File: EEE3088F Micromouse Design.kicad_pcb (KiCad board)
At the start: 2 copper layers, 70 x 78.3 mm, 10 parts, among them J1 Conn_02x16_Odd_Even, J2 Conn_01x02, SW1 SW_SPDT, U1 INA219AxD

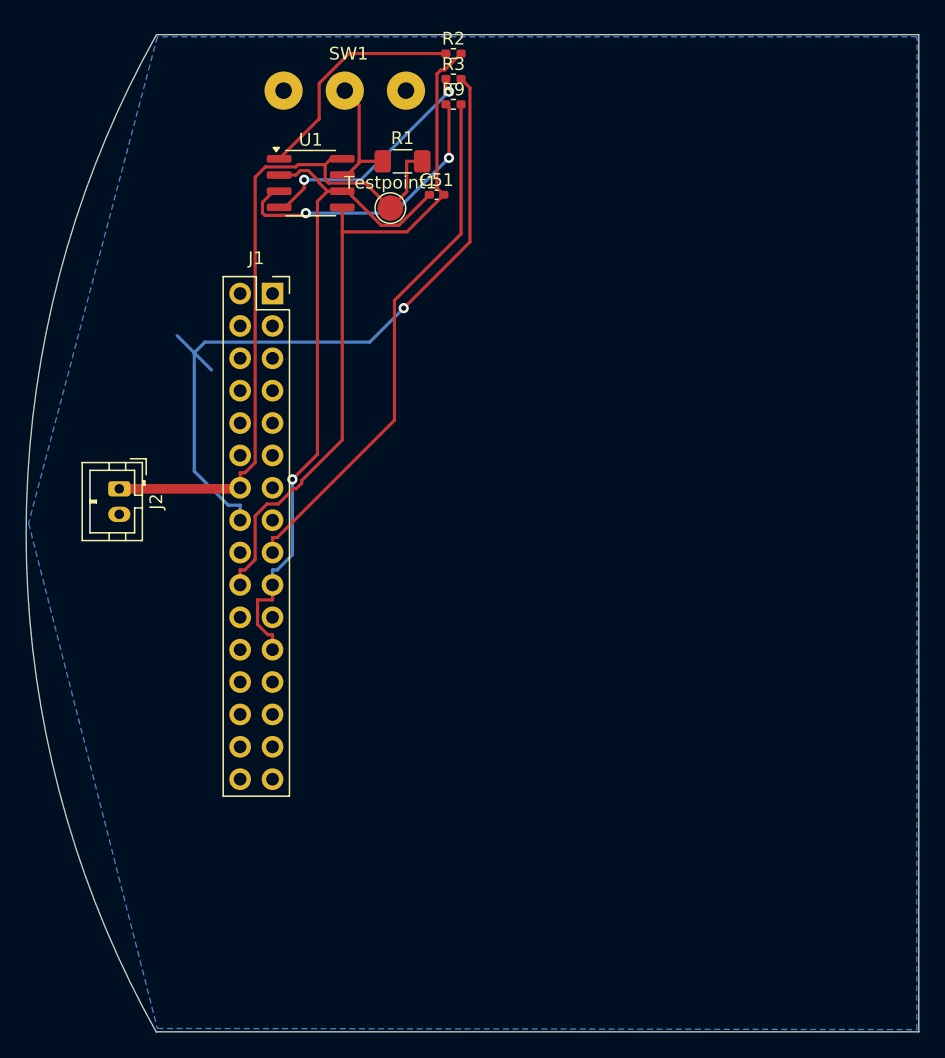
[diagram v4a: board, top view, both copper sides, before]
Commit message: First turnover, changed pcb layout
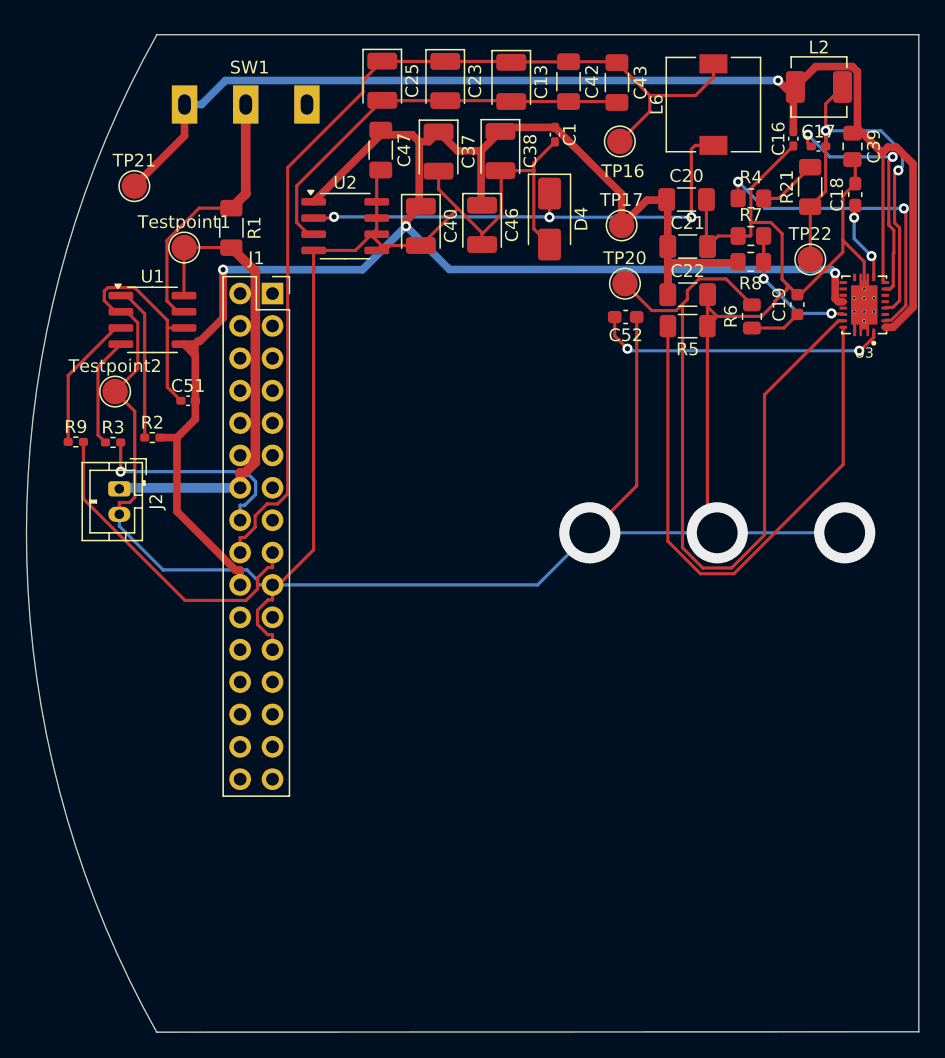
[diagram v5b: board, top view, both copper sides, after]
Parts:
- added C1: 1uF, Capacitor_SMD:C_0402_1005Metric_Pad0.74x0.62mm_HandSolder, F.Cu at (99.0, 77.7)
- added C13: 100uF, Capacitor_Tantalum_SMD:CP_EIA-3528-21_Kemet-B, F.Cu at (95.6, 73.5)
- added C16: 0.1uF, Capacitor_SMD:C_0402_1005Metric_Pad0.74x0.62mm_HandSolder, F.Cu at (117.7, 78.0)
- added C17: 0.1uF, Capacitor_SMD:C_0402_1005Metric_Pad0.74x0.62mm_HandSolder, F.Cu at (119.7, 78.6)
- added C18: 47nF, Capacitor_SMD:C_0603_1608Metric_Pad1.08x0.95mm_HandSolder, F.Cu at (122.6, 82.4)
- added C19: 1nF, Capacitor_SMD:C_0603_1608Metric, F.Cu at (118.0, 91.0)
- added C20: 22uF, Capacitor_SMD:C_1206_3216Metric_Pad1.33x1.80mm_HandSolder, F.Cu at (109.3, 82.8)
- added C21: 22uF, Capacitor_SMD:C_1206_3216Metric_Pad1.33x1.80mm_HandSolder, F.Cu at (109.4, 86.5)
- added C22: 22uF, Capacitor_SMD:C_1206_3216Metric_Pad1.33x1.80mm_HandSolder, F.Cu at (109.4, 90.2)
- added C23: 100uF, Capacitor_Tantalum_SMD:CP_EIA-3528-21_Kemet-B, F.Cu at (90.4, 73.5)
- added C25: 100uF, Capacitor_Tantalum_SMD:CP_EIA-3528-21_Kemet-B, F.Cu at (85.4, 73.4)
- added C37: 100uF, Capacitor_Tantalum_SMD:CP_EIA-3528-21_Kemet-B, F.Cu at (89.9, 79.0)
- added C38: 100uF, Capacitor_Tantalum_SMD:CP_EIA-3528-21_Kemet-B, F.Cu at (94.7, 79.0)
- added C39: 10uF, Capacitor_SMD:C_0805_2012Metric_Pad1.18x1.45mm_HandSolder, F.Cu at (122.3, 78.6)
- added C40: 100uF, Capacitor_Tantalum_SMD:CP_EIA-3528-21_Kemet-B, F.Cu at (88.5, 84.8)
- added C42: 47uF, Capacitor_SMD:C_1206_3216Metric_Pad1.33x1.80mm_HandSolder, F.Cu at (100.1, 73.5)
- added C43: 47uF, Capacitor_SMD:C_1206_3216Metric_Pad1.33x1.80mm_HandSolder, F.Cu at (103.9, 73.6)
- added C46: 100uF, Capacitor_Tantalum_SMD:CP_EIA-3528-21_Kemet-B, F.Cu at (93.3, 84.8)
- added C47: 47uF, Capacitor_SMD:C_1206_3216Metric_Pad1.33x1.80mm_HandSolder, F.Cu at (85.3, 78.9)
- added C52: 2.2uF, Capacitor_SMD:C_0603_1608Metric_Pad1.08x0.95mm_HandSolder, F.Cu at (104.5, 92.0)
- added D4: SS32, Diode_SMD:D_SMA, F.Cu at (98.6, 84.3)
- added L2: 1.2uH, Inductor_SMD:L_Changjiang_FXL0420, F.Cu at (119.7, 73.9)
- added L6: 22uH, Inductor_SMD:L_7.3x7.3_H4.5, F.Cu at (111.4, 75.3)
- added R21: 33k, Resistor_SMD:R_1206_3216Metric_Pad1.30x1.75mm_HandSolder, F.Cu at (119.0, 81.8)
- added R4: 220k, Resistor_SMD:R_0805_2012Metric_Pad1.20x1.40mm_HandSolder, F.Cu at (114.4, 82.7)
- added R5: 100k, Resistor_SMD:R_1206_3216Metric_Pad1.30x1.75mm_HandSolder, F.Cu at (109.4, 92.7)
- added R6: 68k, Resistor_SMD:R_0805_2012Metric, F.Cu at (114.4, 91.9)
- added R7: 47k, Resistor_SMD:R_0805_2012Metric_Pad1.20x1.40mm_HandSolder, F.Cu at (114.4, 85.6)
- added R8: 150k, Resistor_SMD:R_0805_2012Metric_Pad1.20x1.40mm_HandSolder, F.Cu at (114.4, 87.7)
- added TP16: TestPoint, TestPoint:TestPoint_Pad_D2.0mm, F.Cu at (104.1, 78.2)
- added TP17: TestPoint, TestPoint:TestPoint_Pad_D2.0mm, F.Cu at (104.2, 84.8)
- added TP20: TestPoint, TestPoint:TestPoint_Pad_D2.0mm, F.Cu at (104.5, 89.4)
- added TP21: TestPoint, TestPoint:TestPoint_Pad_D2.0mm, F.Cu at (66.0, 81.7)
- added TP22: TestPoint, TestPoint:TestPoint_Pad_D2.0mm, F.Cu at (119.0, 87.5)
- added Testpoint2: TestPoint, TestPoint:TestPoint_Pad_D2.0mm, F.Cu at (64.5, 97.8)
- added U2: XL1509-3.3, Package_SO:SOIC-8_3.9x4.9mm_P1.27mm, F.Cu at (82.5, 84.9)
- added U3: TPS61088RHLR, TPS61088:IC_TPS61088RHLR, F.Cu at (123.3, 91.0)
- SW1: footprint HX_SS12D10G6_Switch:Untitled -> Footprints:SS12D10G4 071
- moved R9 39.7 mm to (61.4, 101.8)
- moved R3 39.1 mm to (64.3, 101.8)
- moved R2 38.3 mm to (67.4, 101.4)
- moved C51 25.3 mm to (70.2, 98.6)
- moved Testpoint1 16.5 mm to (69.9, 86.5)
- moved U1 16.4 mm to (67.4, 92.2)
- moved R1 14.4 mm to (73.6, 85.0), turned to -90 degrees
- moved SW1 7.85 mm to (74.7, 75.3)
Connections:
- J1 pad 18: /3V3 Out -> /3.3V Out
- J2 pad 2: /V_Battery- -> GND
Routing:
- net GND: track 54.6 -> 272.8 mm, vias 1 -> 3
- net /Vcc: track 0.00 -> 101.9 mm, vias 0 -> 1
- net /5V Out: track 55.2 -> 148.8 mm, vias 0 -> 3
- net /3.3V Out: track 0.00 -> 77.3 mm
- net Net-(U3-COMP): track 0.00 -> 60.0 mm
- net Net-(U3-ILIM): track 0.00 -> 46.0 mm
- net /SCLK_INA219: track 57.3 -> 16.9 mm
- net Net-(D4-K): track 0.00 -> 38.7 mm, vias 0 -> 3
- net Net-(U3-SW_4): track 0.00 -> 37.1 mm, vias 0 -> 2
- net Net-(U2-FB): track 0.00 -> 32.6 mm
- net Net-(U3-FSW): track 0.00 -> 25.0 mm, vias 0 -> 2
- net Net-(U3-VCC): track 0.00 -> 23.1 mm, vias 0 -> 2
- net Net-(U3-BOOT): track 0.00 -> 19.8 mm, vias 0 -> 2
- net /V_Battery+: track 54.7 -> 37.3 mm
- net /SDA_INA219: track 41.5 -> 25.4 mm
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- removed copper zone on B.Cu, net (none)
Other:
- outline, holes or cut-outs redrawn

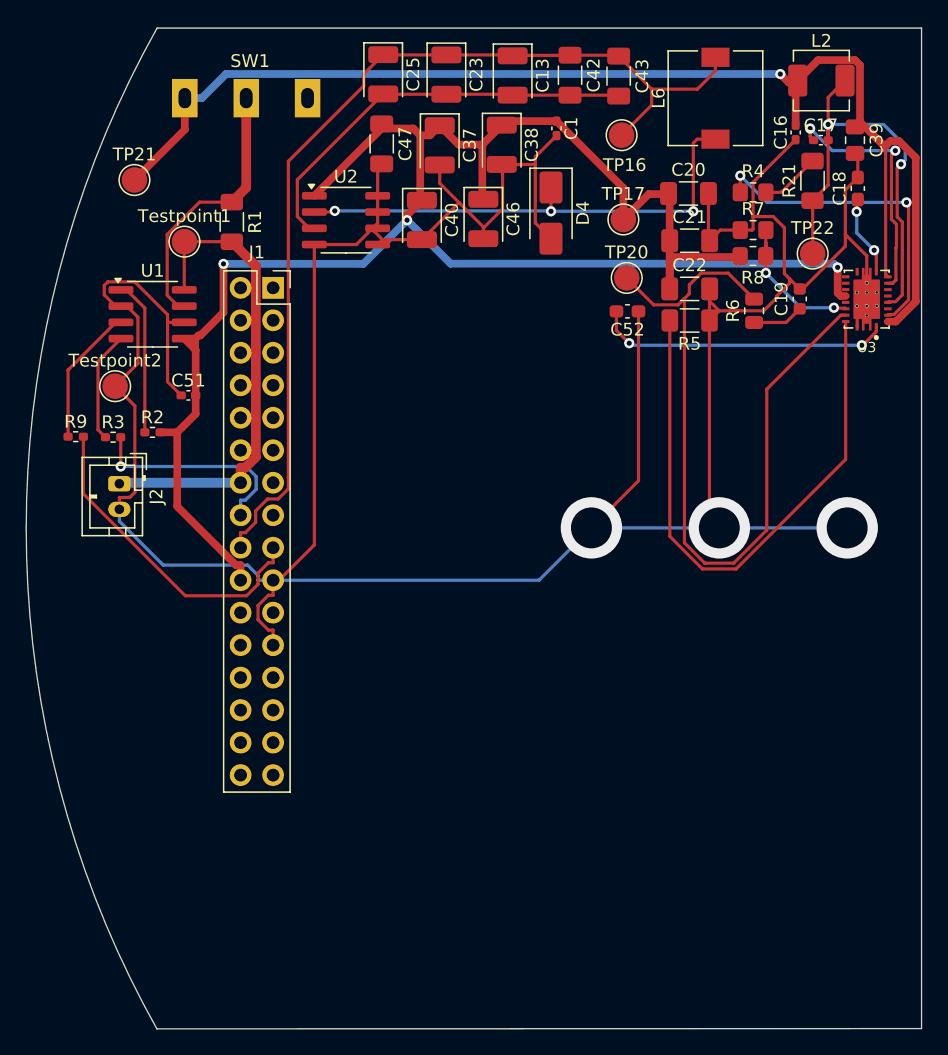
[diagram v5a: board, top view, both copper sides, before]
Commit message: Started routing PCB
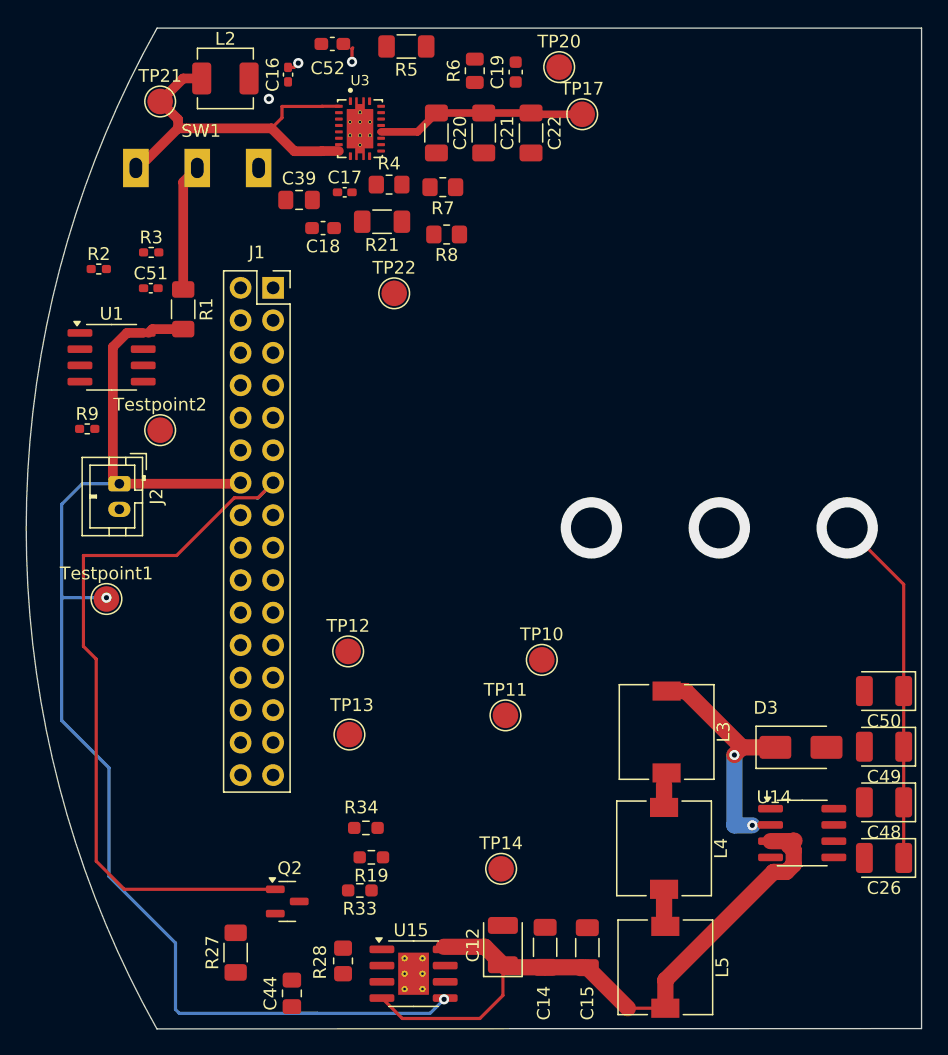
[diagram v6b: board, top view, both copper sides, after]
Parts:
- removed C1: 1uF, Capacitor_SMD:C_0402_1005Metric_Pad0.74x0.62mm_HandSolder
- removed C13, C23, C25, C37, C38, C40, C46: 100uF, Capacitor_Tantalum_SMD:CP_EIA-3528-21_Kemet-B
- removed C42, C43, C47: 47uF, Capacitor_SMD:C_1206_3216Metric_Pad1.33x1.80mm_HandSolder
- removed D4: SS32, Diode_SMD:D_SMA
- removed L6: 22uH, Inductor_SMD:L_7.3x7.3_H4.5
- removed TP16: TestPoint, TestPoint:TestPoint_Pad_D2.0mm
- removed U2: XL1509-3.3, Package_SO:SOIC-8_3.9x4.9mm_P1.27mm
- added C12: 100uF, Capacitor_Tantalum_SMD:CP_EIA-3528-21_Kemet-B, F.Cu at (94.8, 141.5)
- added C14: 47uF, Capacitor_SMD:C_1206_3216Metric_Pad1.33x1.80mm_HandSolder, F.Cu at (98.1, 141.7)
- added C15: 47uF, Capacitor_SMD:C_1206_3216Metric_Pad1.33x1.80mm_HandSolder, F.Cu at (101.4, 141.7)
- added C26: 100uF, Capacitor_Tantalum_SMD:CP_EIA-3528-21_Kemet-B, F.Cu at (124.6, 134.7)
- added C44: 10uF, Capacitor_SMD:C_0805_2012Metric_Pad1.18x1.45mm_HandSolder, F.Cu at (78.3, 145.3)
- added C48: 100uF, Capacitor_Tantalum_SMD:CP_EIA-3528-21_Kemet-B, F.Cu at (124.6, 130.4)
- added C49: 100uF, Capacitor_Tantalum_SMD:CP_EIA-3528-21_Kemet-B, F.Cu at (124.6, 126.0)
- added C50: 100uF, Capacitor_Tantalum_SMD:CP_EIA-3528-21_Kemet-B, F.Cu at (124.6, 121.7)
- added D3: SS32, Diode_SMD:D_SMA, F.Cu at (118.1, 126.1)
- added L3: 22uH, Inductor_SMD:L_7.3x7.3_H4.5, F.Cu at (107.6, 124.9)
- added L4: 22uH, Inductor_SMD:L_7.3x7.3_H4.5, F.Cu at (107.4, 134.0)
- added L5: 22uH, Inductor_SMD:L_7.3x7.3_H4.5, F.Cu at (107.5, 143.3)
- added Q2: AO3400A, Package_TO_SOT_SMD:SOT-23, F.Cu at (77.9, 138.1)
- added R19: 10k, Resistor_SMD:R_0603_1608Metric_Pad0.98x0.95mm_HandSolder, F.Cu at (84.5, 134.7)
- added R27: 4.7k, Resistor_SMD:R_1206_3216Metric_Pad1.30x1.75mm_HandSolder, F.Cu at (73.9, 142.1)
- added R28: 330, Resistor_SMD:R_0805_2012Metric_Pad1.20x1.40mm_HandSolder, F.Cu at (82.3, 142.8)
- added R33: 2.2k, Resistor_SMD:R_0603_1608Metric_Pad0.98x0.95mm_HandSolder, F.Cu at (83.6, 137.3)
- added R34: 270, Resistor_SMD:R_0603_1608Metric_Pad0.98x0.95mm_HandSolder, F.Cu at (84.1, 132.4)
- added TP10: TestPoint, TestPoint:TestPoint_Pad_D2.0mm, F.Cu at (97.8, 119.2)
- added TP11: TestPoint, TestPoint:TestPoint_Pad_D2.0mm, F.Cu at (95.0, 123.6)
- added TP12: TestPoint, TestPoint:TestPoint_Pad_D2.0mm, F.Cu at (82.7, 118.6)
- added TP13: TestPoint, TestPoint:TestPoint_Pad_D2.0mm, F.Cu at (82.8, 125.1)
- added TP14: TestPoint, TestPoint:TestPoint_Pad_D2.0mm, F.Cu at (94.7, 135.6)
- added U14: XL1509-5.0, Package_SO:SOIC-8_3.9x4.9mm_P1.27mm, F.Cu at (118.2, 132.8)
- added U15: TP4056-42-ESOP8, Package_SO:SOIC-8-1EP_3.9x4.9mm_P1.27mm_EP2.41x3.3mm_ThermalVias, F.Cu at (87.8, 143.8)
- moved L2 46.6 mm to (73.1, 73.8)
- moved C39 43.7 mm to (78.9, 83.3), turned to 0 degrees
- moved C18 41.9 mm to (80.7, 85.5), turned to 180 degrees
- moved U3 41.8 mm to (83.6, 77.7), turned to 0 degrees
- moved C16 39.9 mm to (78.0, 73.5), turned to -90 degrees
- moved C17 37.4 mm to (82.4, 82.7)
- moved R21 33.8 mm to (85.4, 85.0), turned to 180 degrees
- moved TP22 32.9 mm to (86.3, 90.6)
- moved C52 31.1 mm to (81.5, 71.1)
- moved R5 30.8 mm to (87.3, 71.3)
- moved R6 28.8 mm to (92.6, 73.2)
- moved Testpoint1 28.6 mm to (63.8, 114.5)
- moved R4 28.5 mm to (85.9, 82.1)
- moved C19 28.4 mm to (95.8, 73.3)
- moved R7 24.5 mm to (90.1, 82.3), turned to 180 degrees
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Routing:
- net GND: track 272.8 -> 29.8 mm, vias 3 -> 5
- net /5V Out: track 148.8 -> 17.2 mm, vias 3 -> 0
- net /3.3V Out: track 77.3 -> 0.00 mm
- net /Vcc: track 101.9 -> 31.1 mm, vias 1 -> 0
- net /V_Battery+: track 37.3 -> 103.3 mm, vias 0 -> 2
- net Net-(U3-COMP): track 60.0 -> 0.00 mm
- net /FAST_CHARGE_CTRL: track 0.00 -> 58.2 mm
- net /Stepped Down 5V: track 0.00 -> 52.7 mm
- net Net-(U3-ILIM): track 46.0 -> 0.00 mm
- net Net-(D4-K): track 38.7 -> 0.00 mm, vias 3 -> 0
- net Net-(U3-SW_4): track 37.1 -> 0.05 mm, vias 2 -> 1
- net Net-(U2-FB): track 32.6 -> 0.00 mm
- net /SDA_INA219: track 25.4 -> 0.00 mm
- net Net-(U3-FSW): track 25.0 -> 0.00 mm, vias 2 -> 0
- net Net-(U3-VCC): track 23.1 -> 0.00 mm, vias 2 -> 0
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
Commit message: Finishing off
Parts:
- removed TP13, Testpoint2: TestPoint, TestPoint:TestPoint_Pad_D2.0mm
- added C1: 1uF, Capacitor_SMD:C_0402_1005Metric_Pad0.74x0.62mm_HandSolder, F.Cu at (108.9, 72.5)
- added C13: 100uF, Capacitor_Tantalum_SMD:CP_EIA-3528-21_Kemet-B, F.Cu at (124.4, 82.3)
- added C23: 100uF, Capacitor_Tantalum_SMD:CP_EIA-3528-21_Kemet-B, F.Cu at (124.4, 92.0)
- added C24: 1uF, Capacitor_SMD:C_0402_1005Metric_Pad0.74x0.62mm_HandSolder, F.Cu at (125.7, 133.3)
- added C25: 100uF, Capacitor_Tantalum_SMD:CP_EIA-3528-21_Kemet-B, F.Cu at (124.4, 87.2)
- added C27: 1uF, Capacitor_SMD:C_0402_1005Metric_Pad0.74x0.62mm_HandSolder, F.Cu at (101.6, 88.4)
- added C28: 10nF, Capacitor_SMD:C_0603_1608Metric, F.Cu at (103.5, 104.4)
- added C29: 2.2uF, Capacitor_SMD:C_0603_1608Metric_Pad1.08x0.95mm_HandSolder, F.Cu at (105.5, 97.1)
- added C30: 10nF, Capacitor_SMD:C_0603_1608Metric, F.Cu at (100.7, 125.8)
- added C31: 2.2uF, Capacitor_SMD:C_0603_1608Metric_Pad1.08x0.95mm_HandSolder, F.Cu at (102.5, 118.8)
- added C32: 1uF, Capacitor_SMD:C_0402_1005Metric_Pad0.74x0.62mm_HandSolder, F.Cu at (101.5, 85.9)
- added C33: 1uF, Capacitor_SMD:C_0402_1005Metric_Pad0.74x0.62mm_HandSolder, F.Cu at (105.4, 88.2)
- added C34: 1uF, Capacitor_SMD:C_0402_1005Metric_Pad0.74x0.62mm_HandSolder, F.Cu at (103.0, 95.6)
- added C35: 1nF, Capacitor_SMD:C_0603_1608Metric, F.Cu at (106.6, 91.0)
- added C36: 1nF, Capacitor_SMD:C_0603_1608Metric, F.Cu at (106.6, 94.1)
- added C37: 100uF, Capacitor_Tantalum_SMD:CP_EIA-3528-21_Kemet-B, F.Cu at (110.8, 90.2)
- added C38: 100uF, Capacitor_Tantalum_SMD:CP_EIA-3528-21_Kemet-B, F.Cu at (119.9, 90.1)
- added C40: 100uF, Capacitor_Tantalum_SMD:CP_EIA-3528-21_Kemet-B, F.Cu at (115.7, 85.7)
- added C41: 10uF, Capacitor_SMD:C_0805_2012Metric_Pad1.18x1.45mm_HandSolder, F.Cu at (101.3, 122.7)
- added C42: 47uF, Capacitor_SMD:C_1206_3216Metric_Pad1.33x1.80mm_HandSolder, F.Cu at (125.0, 96.5)
- added C43: 47uF, Capacitor_SMD:C_1206_3216Metric_Pad1.33x1.80mm_HandSolder, F.Cu at (121.1, 96.5)
- added C45: 10uF, Capacitor_SMD:C_0805_2012Metric_Pad1.18x1.45mm_HandSolder, F.Cu at (105.3, 100.4)
- added C46: 100uF, Capacitor_Tantalum_SMD:CP_EIA-3528-21_Kemet-B, F.Cu at (115.6, 80.5)
- added C47: 47uF, Capacitor_SMD:C_1206_3216Metric_Pad1.33x1.80mm_HandSolder, F.Cu at (115.4, 90.2)
- added D4: SS32, Diode_SMD:D_SMA, F.Cu at (114.6, 73.7)
- added HV: TestPoint, TestPoint:TestPoint_Pad_D2.0mm, F.Cu at (65.2, 118.8)
- added J3: TYPE-C-31-M-12, Footprints:HRO_TYPE-C-31-M-12, F.Cu at (120.3, 144.9)
- added L6: 22uH, Inductor_SMD:L_7.3x7.3_H4.5, F.Cu at (122.9, 75.2)
- added R15: 1k, Resistor_SMD:R_0402_1005Metric_Pad0.72x0.64mm_HandSolder, F.Cu at (125.7, 137.8)
- added R16: 6.8k, Resistor_SMD:R_0805_2012Metric_Pad1.20x1.40mm_HandSolder, F.Cu at (114.2, 135.4)
- added R18: 10k, Resistor_SMD:R_0603_1608Metric_Pad0.98x0.95mm_HandSolder, F.Cu at (120.2, 130.5)
- added R26: 1, Resistor_SMD:R_1206_3216Metric_Pad1.30x1.75mm_HandSolder, F.Cu at (89.5, 94.9)
- added R29: 0.82, Resistor_SMD:R_0603_1608Metric_Pad0.98x0.95mm_HandSolder, F.Cu at (91.8, 125.8)
- added R30: 0.82, Resistor_SMD:R_0603_1608Metric_Pad0.98x0.95mm_HandSolder, F.Cu at (88.8, 125.8)
- added R31: 0.82, Resistor_SMD:R_0603_1608Metric_Pad0.98x0.95mm_HandSolder, F.Cu at (96.8, 112.8)
- added R32: 0.82, Resistor_SMD:R_0603_1608Metric_Pad0.98x0.95mm_HandSolder, F.Cu at (85.8, 125.7)
- added R35: 1, Resistor_SMD:R_1206_3216Metric_Pad1.30x1.75mm_HandSolder, F.Cu at (93.3, 95.1)
- added Testpoint1: TestPoint, TestPoint:TestPoint_Pad_D2.0mm, F.Cu at (111.9, 104.3)
- added U11: DRV8833PW, Package_SO:TSSOP-16_4.4x5mm_P0.65mm, F.Cu at (96.2, 101.0)
- added U12: DRV8833PW, Package_SO:TSSOP-16_4.4x5mm_P0.65mm, F.Cu at (95.2, 120.1)
- added U13: AP22966DC8-7, AP22966DC8-7:IC_AP22966DC8-7, F.Cu at (102.0, 91.9)
- added U2: XL1509-3.3, Package_SO:SOIC-8_3.9x4.9mm_P1.27mm, F.Cu at (107.1, 81.2)
- added U9: CH224K, Package_SO:SSOP-10-1EP_3.9x4.9mm_P1mm_EP2.1x3.3mm, F.Cu at (119.3, 135.8)
- moved 5VStep 18.1 mm to (101.5, 137.0)
- moved CRGnd 17.2 mm to (93.5, 132.0)
- moved CR1 13.5 mm to (93.5, 137.0)
- moved TP22 10.7 mm to (94.3, 83.5)
- moved U14 7.73 mm to (117.5, 125.1)
- moved C26 7.73 mm to (123.9, 127.0)
- moved C48 7.73 mm to (123.9, 122.7)
- moved C49 7.73 mm to (123.9, 118.3)
- moved C50 7.73 mm to (123.9, 114.0)
- moved D3 7.73 mm to (117.4, 118.4)
- moved CR2 6.32 mm to (88.5, 137.0)
- renumbered TP10 to 5VStep, TP11 to CR1, TP14 to CR2, TP12 to CRGnd, Testpoint1 to vBat
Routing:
- net GND: track 29.8 -> 548.2 mm, vias 5 -> 11
- net /5V Out: track 17.2 -> 185.0 mm, vias 0 -> 3
- net /HV: track 0.00 -> 113.1 mm, vias 0 -> 4
- net /3.3V Out: track 0.00 -> 82.4 mm, vias 0 -> 1
- net /V_Battery+: track 103.3 -> 183.9 mm, vias 2 -> 6
- net /MOTOR1_A_OUT: track 0.00 -> 67.5 mm, vias 0 -> 1
- net /EXT_LOAD1_OUT: track 0.00 -> 62.2 mm, vias 0 -> 1
- net /CTRL_EXT_LOAD1: track 0.00 -> 57.8 mm, vias 0 -> 9
- net Net-(U2-FB): track 0.00 -> 55.0 mm, vias 0 -> 2
- net /Motor4_B_OUT: track 0.00 -> 54.1 mm, vias 0 -> 3
- net /MOTOR4_CTRL2: track 0.00 -> 52.5 mm, vias 0 -> 2
- net /MOTOR1_B_OUT: track 0.00 -> 51.1 mm, vias 0 -> 2
- net /Motor4_A_OUT: track 0.00 -> 45.2 mm
- net /MOTOR4_CTRL1: track 0.00 -> 45.2 mm, vias 0 -> 2
- net /MOTOR1_CTRL2: track 0.00 -> 43.8 mm, vias 0 -> 1
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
